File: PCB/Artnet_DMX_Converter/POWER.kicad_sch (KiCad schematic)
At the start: 23 parts, among them IC1 NPM1300-QEAA-R7

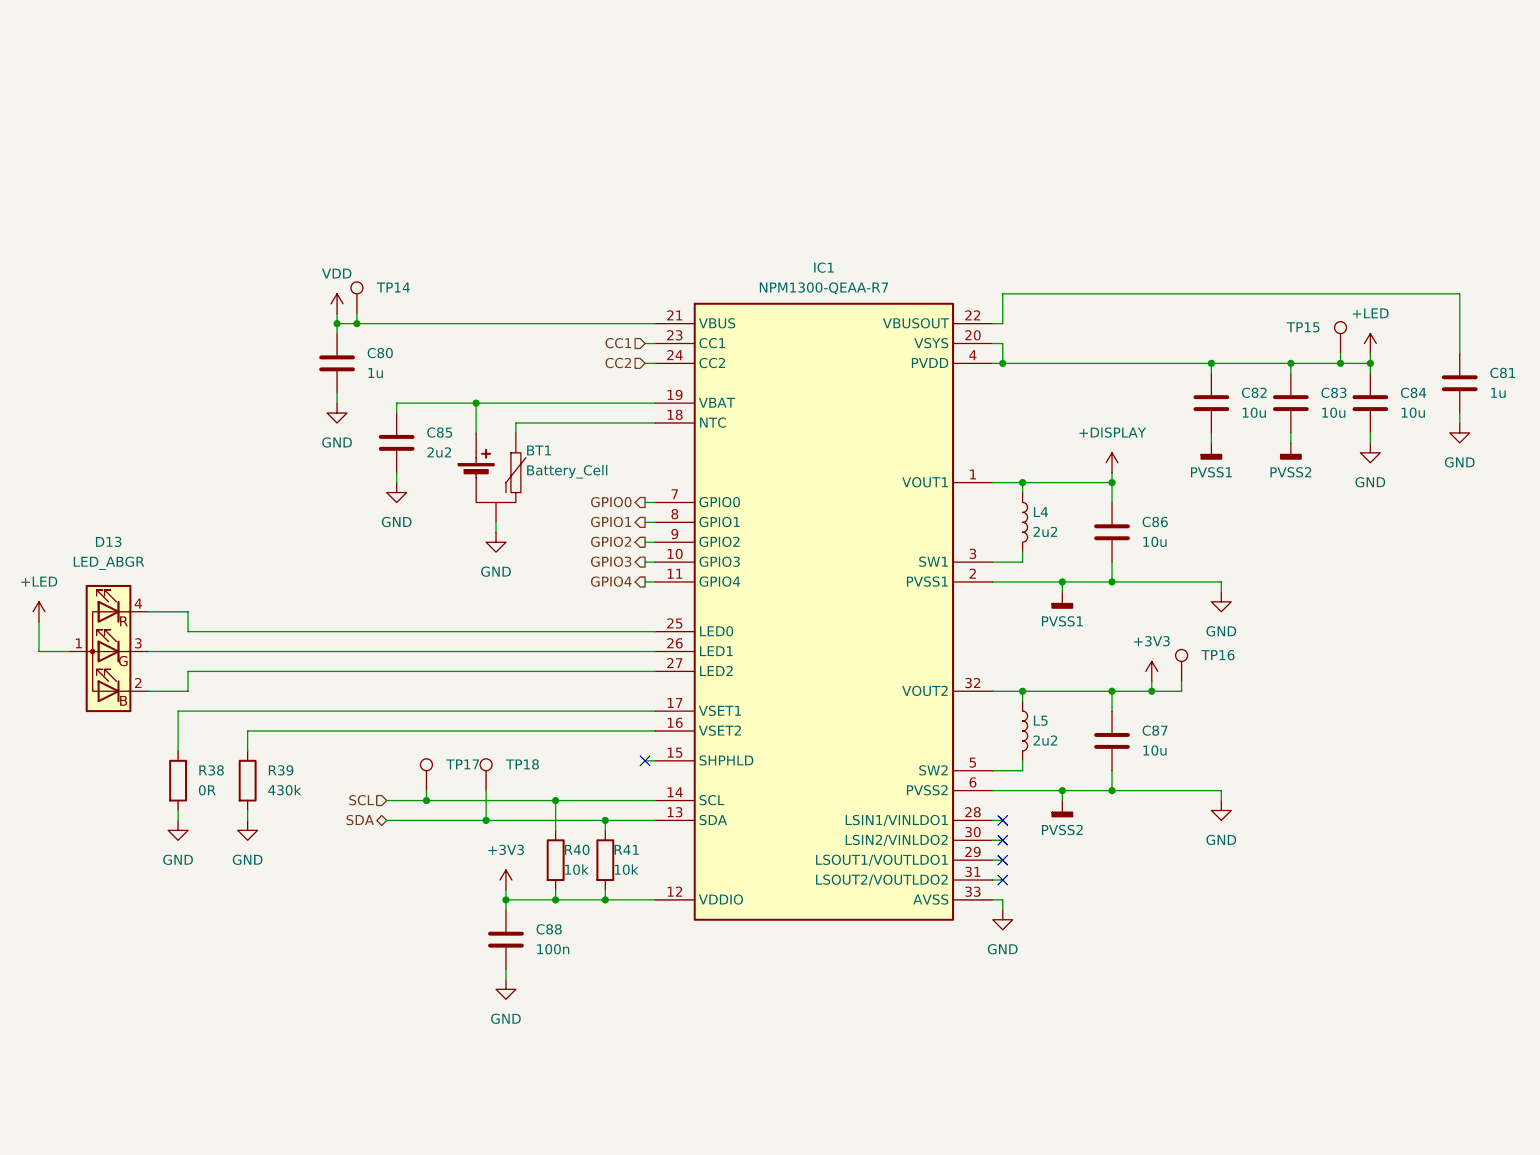
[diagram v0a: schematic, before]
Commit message: Fixed allot of problems
Added a new LDO for the 3.3V rail to support the load i miscalculated 💀
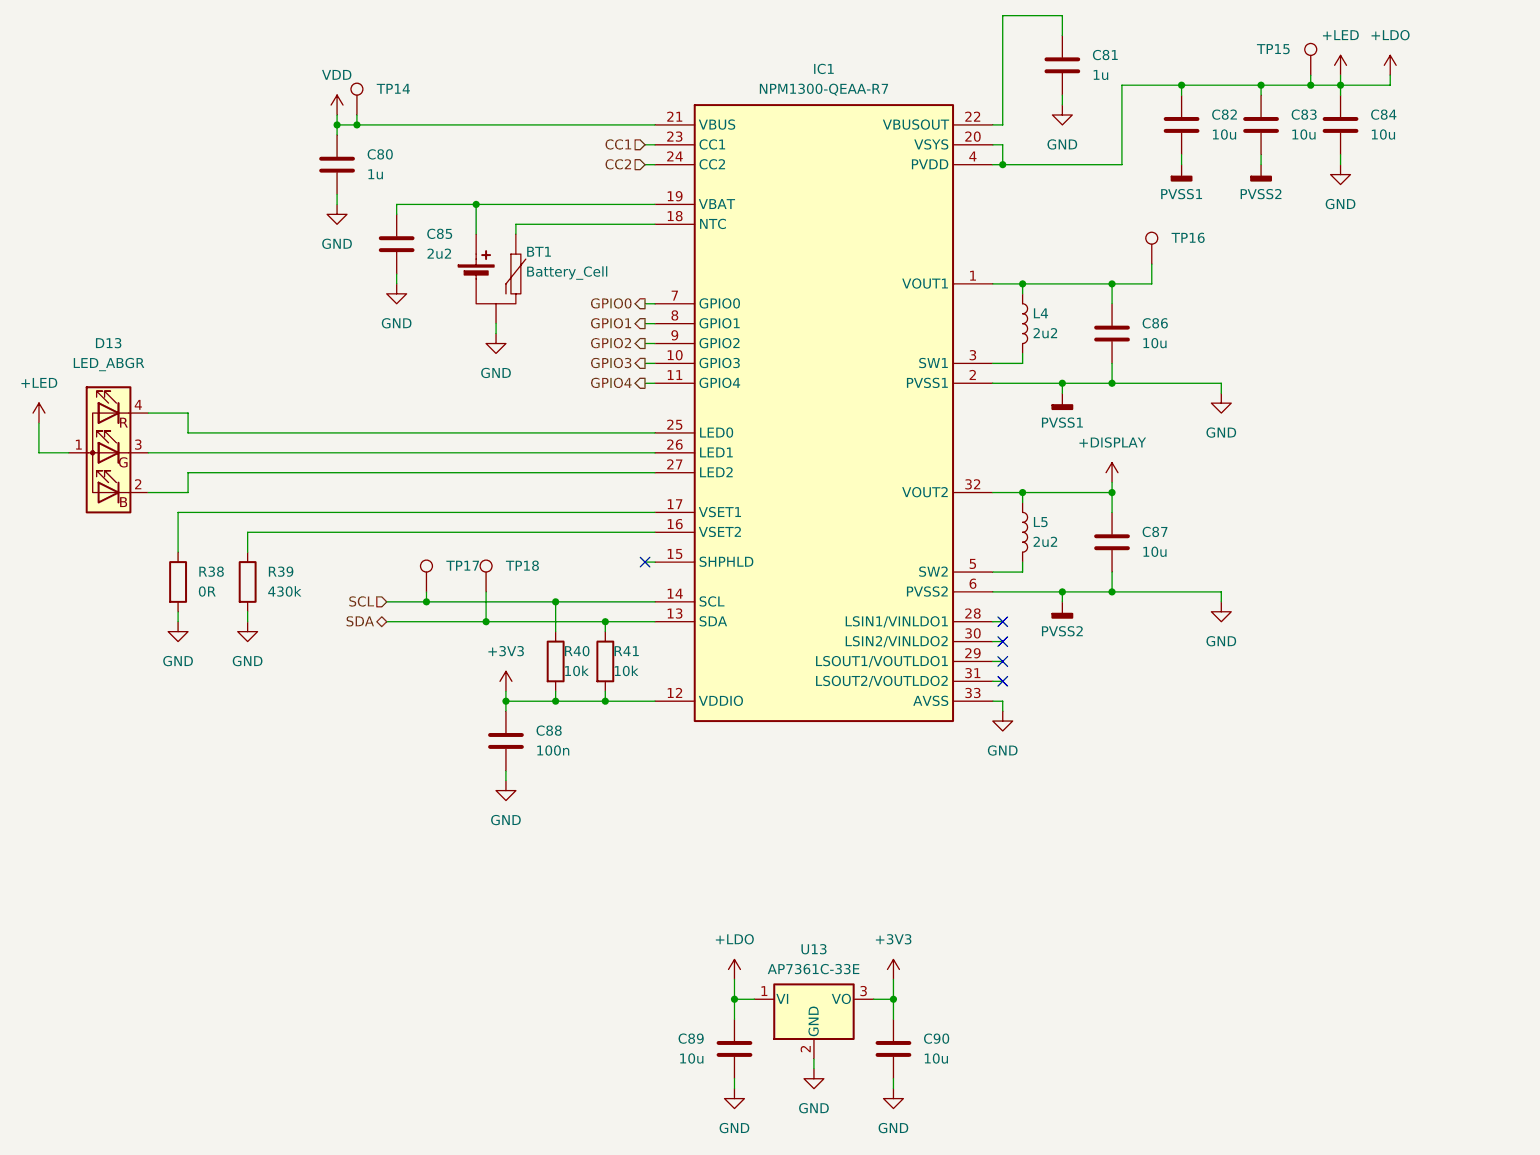
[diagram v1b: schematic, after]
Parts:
- added C89, C90: 10u, Capacitor_SMD:C_0603_1608Metric, symbol Device:C
- added U13: AP7361C-33E, Package_TO_SOT_SMD:SOT-223-3_TabPin2, symbol Regulator_Linear:AP7361C-33E
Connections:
- net +3V3: now also C90.1, U13.3 (VO); no longer C87.1, IC1.32 (VOUT2), L5.1, TP16.1
- net +DISPLAY: now also C87.1, IC1.32 (VOUT2), L5.1; no longer C86.1, IC1.1 (VOUT1), L4.1
- net GND: now also C89.2, C90.2, U13.2 (GND)
- net +LED renamed +LDO
- net +LDO: now also C89.1, U13.1 (VI)
- new net: C86.1, IC1.1 (VOUT1), L4.1, TP16.1
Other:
- moved on the sheet: BT1, C80, C81, C82, C83, C84, C85, C86, C87, C88, D13, IC1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

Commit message: Testpoints and GND1 Fill
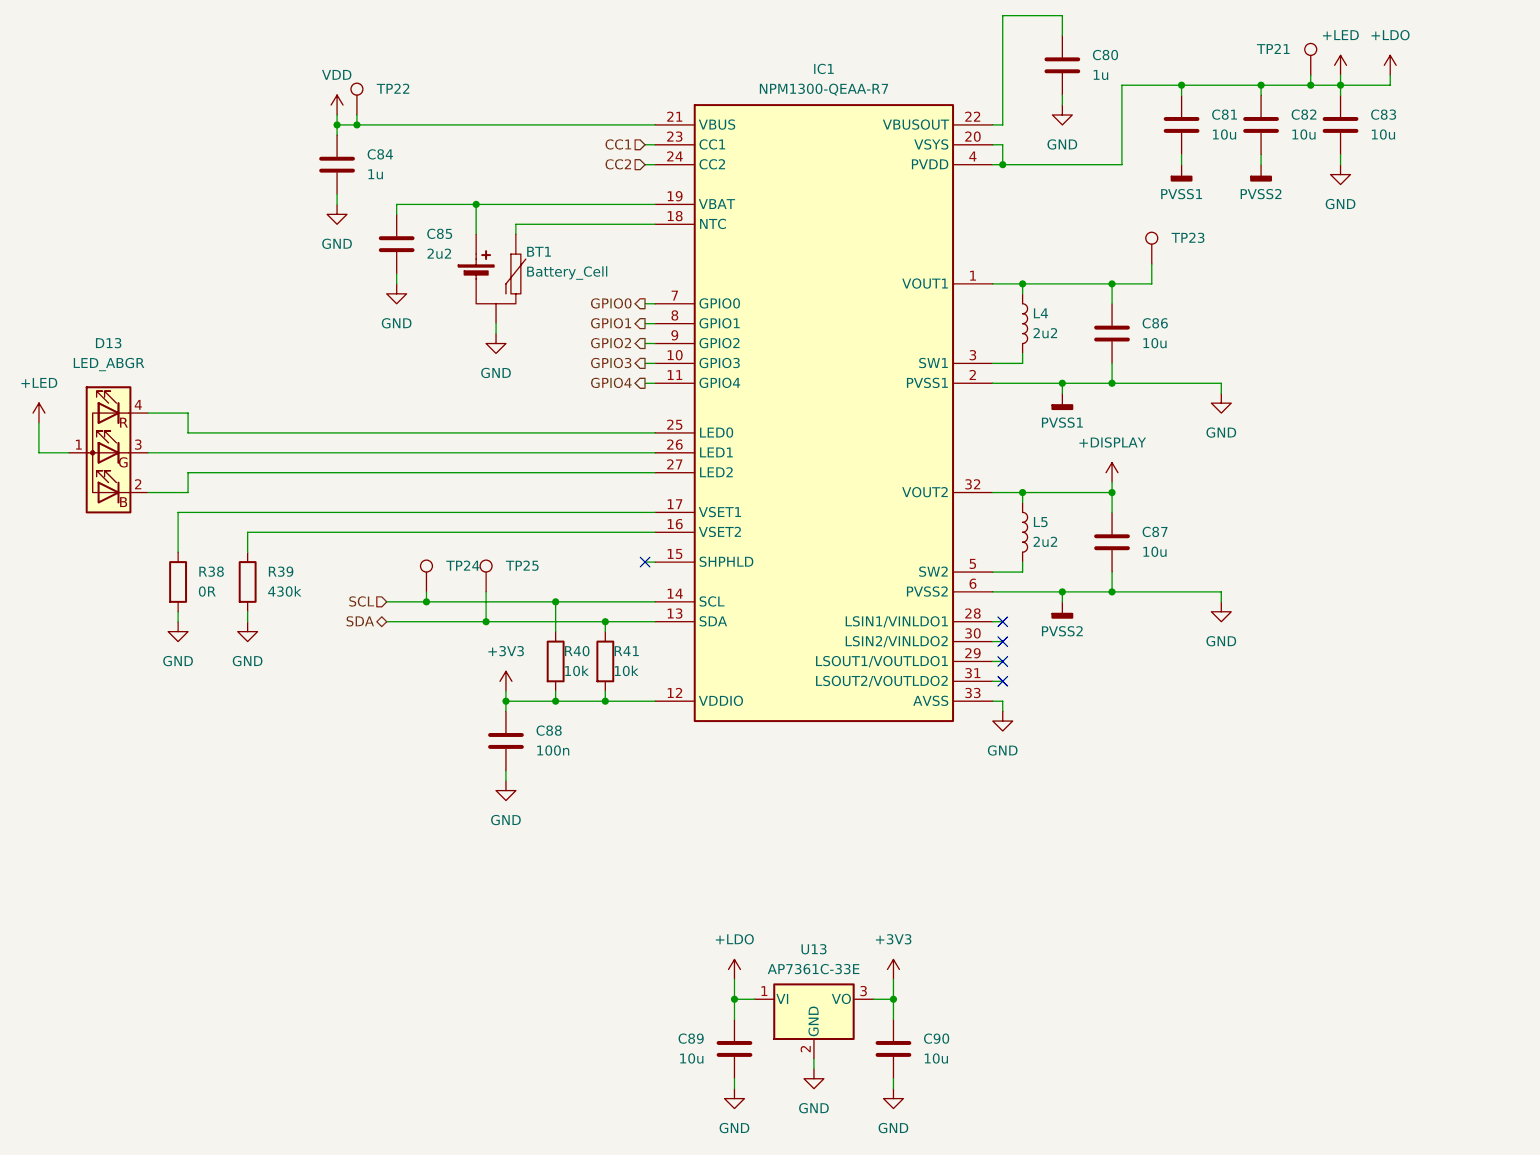
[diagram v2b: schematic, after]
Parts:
- renumbered C81 to C80, C82 to C81, C83 to C82, C84 to C83, C80 to C84, TP15 to TP21, TP14 to TP22, TP16 to TP23, TP17 to TP24, TP18 to TP25
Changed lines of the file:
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@@
 		(dnp no)
 		(fields_autoplaced yes)
-		(property "Reference" "C84"
+		(property "Reference" "C83"
 			(at 203.2 36.8299 0)
 			(effects
@@
 			(project "Artnet_DMX_Converter"
 				(path "/7d5b1976-98b3-4e47-ae52-3fe360235ea3/880ca6d5-39db-482c-a50d-e019dbd8a609"
-					(reference "C84")
+					(reference "C83")
 					(unit 1)
 				)
@@
 		(dnp no)
 		(fields_autoplaced yes)
-		(property "Reference" "#PWR0111"
+		(property "Reference" "#PWR0114"
 			(at 71.12 40.64 0)
 			(effects
@@
 			(project ""
 				(path "/7d5b1976-98b3-4e47-ae52-3fe360235ea3/880ca6d5-39db-482c-a50d-e019dbd8a609"
-					(reference "#PWR0111")
+					(reference "#PWR0114")
 					(unit 1)
 				)
@@
 		(on_board yes)
 		(dnp no)
-		(property "Reference" "#PWR0140"
+		(property "Reference" "#PWR0112"
 			(at 205.74 35.56 0)
 			(effects
@@
 			(project "Artnet_DMX_Converter"
 				(path "/7d5b1976-98b3-4e47-ae52-3fe360235ea3/880ca6d5-39db-482c-a50d-e019dbd8a609"
-					(reference "#PWR0140")
+					(reference "#PWR0112")
 					(unit 1)
 				)
@@
 		(on_board yes)
 		(dnp no)
-		(property "Reference" "TP14"
+		(property "Reference" "TP22"
 			(at 76.2 33.5279 0)
 			(effects
@@
 			(project "Artnet_DMX_Converter"
 				(path "/7d5b1976-98b3-4e47-ae52-3fe360235ea3/880ca6d5-39db-482c-a50d-e019dbd8a609"
-					(reference "TP14")
+					(reference "TP22")
 					(unit 1)
 				)
@@
 		(on_board yes)
 		(dnp no)
-		(property "Reference" "TP15"
+		(property "Reference" "TP21"
 			(at 193.04 28.4479 0)
 			(effects
@@
 			(project "Artnet_DMX_Converter"
 				(path "/7d5b1976-98b3-4e47-ae52-3fe360235ea3/880ca6d5-39db-482c-a50d-e019dbd8a609"
-					(reference "TP15")
+					(reference "TP21")
 					(unit 1)
 				)
@@
 		(dnp no)
 		(fields_autoplaced yes)
-		(property "Reference" "C83"
+		(property "Reference" "C82"
 			(at 193.04 36.8299 0)
 			(effects
@@
 			(project "Artnet_DMX_Converter"
 				(path "/7d5b1976-98b3-4e47-ae52-3fe360235ea3/880ca6d5-39db-482c-a50d-e019dbd8a609"
-					(reference "C83")
+					(reference "C82")
 					(unit 1)
 				)
@@
 		(dnp no)
 		(fields_autoplaced yes)
-		(property "Reference" "#PWR0139"
+		(property "Reference" "#PWR0136"
 			(at 142.24 167.64 0)
 			(effects
@@
 			(project "Artnet_DMX_Converter"
 				(path "/7d5b1976-98b3-4e47-ae52-3fe360235ea3/880ca6d5-39db-482c-a50d-e019dbd8a609"
-					(reference "#PWR0139")
+					(reference "#PWR0136")
 					(unit 1)
 				)
@@
 		(on_board yes)
 		(dnp no)
-		(property "Reference" "TP18"
+		(property "Reference" "TP25"
 			(at 92.71 94.4879 0)
 			(effects
@@
 			(project "Artnet_DMX_Converter"
 				(path "/7d5b1976-98b3-4e47-ae52-3fe360235ea3/880ca6d5-39db-482c-a50d-e019dbd8a609"
-					(reference "TP18")
+					(reference "TP25")
 					(unit 1)
 				)
@@
 		(on_board yes)
 		(dnp no)
-		(property "Reference" "TP16"
+		(property "Reference" "TP23"
 			(at 177.8 52.5779 0)
 			(effects
@@
 			(project "Artnet_DMX_Converter"
 				(path "/7d5b1976-98b3-4e47-ae52-3fe360235ea3/880ca6d5-39db-482c-a50d-e019dbd8a609"
-					(reference "TP16")
+					(reference "TP23")
 					(unit 1)
 				)
@@
 		(dnp no)
 		(fields_autoplaced yes)
-		(property "Reference" "#PWR0137"
+		(property "Reference" "#PWR0134"
 			(at 132.08 165.1 0)
 			(effects
@@
 			(project ""
 				(path "/7d5b1976-98b3-4e47-ae52-3fe360235ea3/880ca6d5-39db-482c-a50d-e019dbd8a609"
-					(reference "#PWR0137")
+					(reference "#PWR0134")
 					(unit 1)
 				)
@@
 		(on_board yes)
 		(dnp no)
-		(property "Reference" "TP17"
+		(property "Reference" "TP24"
 			(at 85.09 94.4879 0)
 			(effects
@@
 			(project "Artnet_DMX_Converter"
 				(path "/7d5b1976-98b3-4e47-ae52-3fe360235ea3/880ca6d5-39db-482c-a50d-e019dbd8a609"
-					(reference "TP17")
+					(reference "TP24")
 					(unit 1)
 				)
@@
 		(dnp no)
 		(fields_autoplaced yes)
-		(property "Reference" "C80"
+		(property "Reference" "C84"
 			(at 74.93 41.9099 0)
 			(effects
@@
 			(project "Artnet_DMX_Converter"
 				(path "/7d5b1976-98b3-4e47-ae52-3fe360235ea3/880ca6d5-39db-482c-a50d-e019dbd8a609"
-					(reference "C80")
+					(reference "C84")
 					(unit 1)
 				)
@@
 		(dnp no)
 		(fields_autoplaced yes)
-		(property "Reference" "#PWR0118"
+		(property "Reference" "#PWR0124"
 			(at 170.18 87.63 0)
 			(effects
@@
 			(project "Artnet_DMX_Converter"
 				(path "/7d5b1976-98b3-4e47-ae52-3fe360235ea3/880ca6d5-39db-482c-a50d-e019dbd8a609"
-					(reference "#PWR0118")
+					(reference "#PWR0124")
 					(unit 1)
 				)
@@
 		(dnp no)
 		(fields_autoplaced yes)
-		(property "Reference" "C81"
+		(property "Reference" "C80"
 			(at 167.64 29.2099 0)
 			(effects
@@
 			(project "Artnet_DMX_Converter"
 				(path "/7d5b1976-98b3-4e47-ae52-3fe360235ea3/880ca6d5-39db-482c-a50d-e019dbd8a609"
-					(reference "C81")
+					(reference "C80")
 					(unit 1)
 				)
@@
 		(dnp no)
 		(fields_autoplaced yes)
-		(property "Reference" "C82"
+		(property "Reference" "C81"
 			(at 182.88 36.8299 0)
 			(effects
@@
 			(project "Artnet_DMX_Converter"
 				(path "/7d5b1976-98b3-4e47-ae52-3fe360235ea3/880ca6d5-39db-482c-a50d-e019dbd8a609"
-					(reference "C82")
+					(reference "C81")
 					(unit 1)
 				)
@@
 		(dnp no)
 		(fields_autoplaced yes)
-		(property "Reference" "#PWR0124"
+		(property "Reference" "#PWR0133"
 			(at 142.24 151.13 0)
 			(effects
@@
 			(project ""
 				(path "/7d5b1976-98b3-4e47-ae52-3fe360235ea3/880ca6d5-39db-482c-a50d-e019dbd8a609"
-					(reference "#PWR0124")
+					(reference "#PWR0133")
 					(unit 1)
 				)
@@
 		(on_board yes)
 		(dnp no)
-		(property "Reference" "#PWR0141"
+		(property "Reference" "#PWR0132"
 			(at 121.92 151.13 0)
 			(effects
@@
 			(project "Artnet_DMX_Converter"
 				(path "/7d5b1976-98b3-4e47-ae52-3fe360235ea3/880ca6d5-39db-482c-a50d-e019dbd8a609"
-					(reference "#PWR0141")
+					(reference "#PWR0132")
 					(unit 1)
 				)
@@
 		(on_board yes)
 		(dnp no)
-		(property "Reference" "#PWR0112"
+		(property "Reference" "#PWR0111"
 			(at 199.39 35.56 0)
 			(effects
@@
 			(project ""
 				(path "/7d5b1976-98b3-4e47-ae52-3fe360235ea3/880ca6d5-39db-482c-a50d-e019dbd8a609"
-					(reference "#PWR0112")
+					(reference "#PWR0111")
 					(unit 1)
 				)
@@
 		(dnp no)
 		(fields_autoplaced yes)
-		(property "Reference" "#PWR0114"
+		(property "Reference" "#PWR0113"
 			(at 163.83 41.91 0)
 			(effects
@@
 			(project "Artnet_DMX_Converter"
 				(path "/7d5b1976-98b3-4e47-ae52-3fe360235ea3/880ca6d5-39db-482c-a50d-e019dbd8a609"
-					(reference "#PWR0114")
+					(reference "#PWR0113")
 					(unit 1)
 				)
@@
 		(dnp no)
 		(fields_autoplaced yes)
-		(property "Reference" "#PWR0138"
+		(property "Reference" "#PWR0135"
 			(at 121.92 167.64 0)
 			(effects
@@
 			(project "Artnet_DMX_Converter"
 				(path "/7d5b1976-98b3-4e47-ae52-3fe360235ea3/880ca6d5-39db-482c-a50d-e019dbd8a609"
-					(reference "#PWR0138")
+					(reference "#PWR0135")
 					(unit 1)
 				)
@@
 		(dnp no)
 		(fields_autoplaced yes)
-		(property "Reference" "#PWR0113"
+		(property "Reference" "#PWR0118"
 			(at 71.12 54.61 0)
 			(effects
@@
 			(project "Artnet_DMX_Converter"
 				(path "/7d5b1976-98b3-4e47-ae52-3fe360235ea3/880ca6d5-39db-482c-a50d-e019dbd8a609"
-					(reference "#PWR0113")
+					(reference "#PWR0118")
 					(unit 1)
 				)
